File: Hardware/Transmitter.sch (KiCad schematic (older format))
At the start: 26 parts, among them U2 ADF7012, X1 VCXO

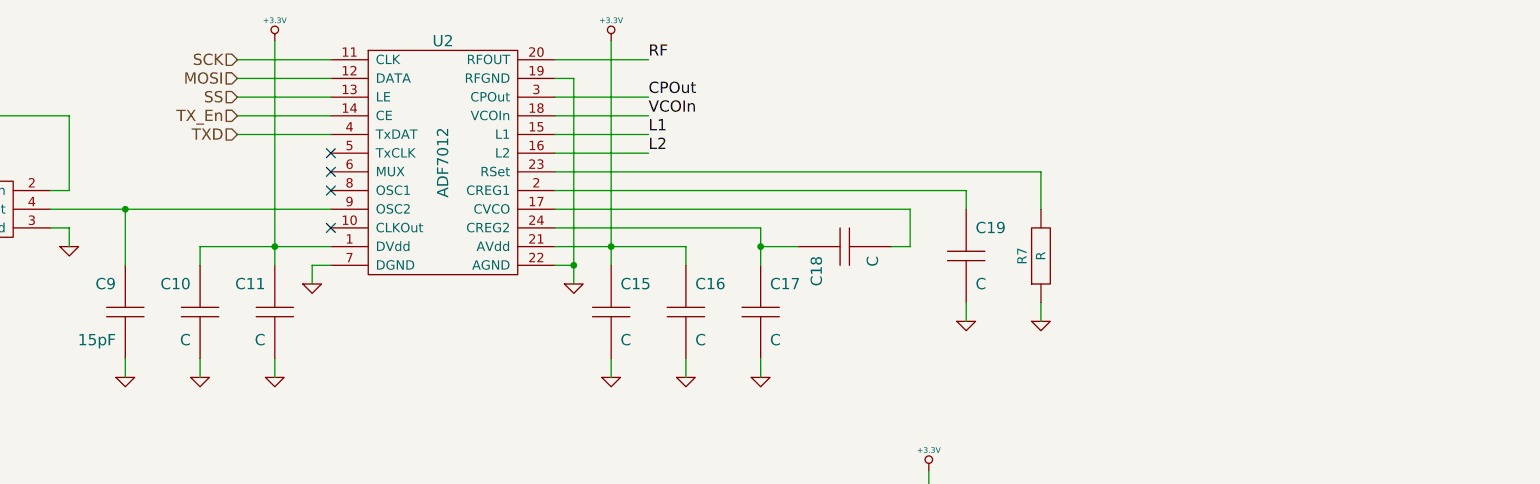
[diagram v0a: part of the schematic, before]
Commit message: Transmitter support components
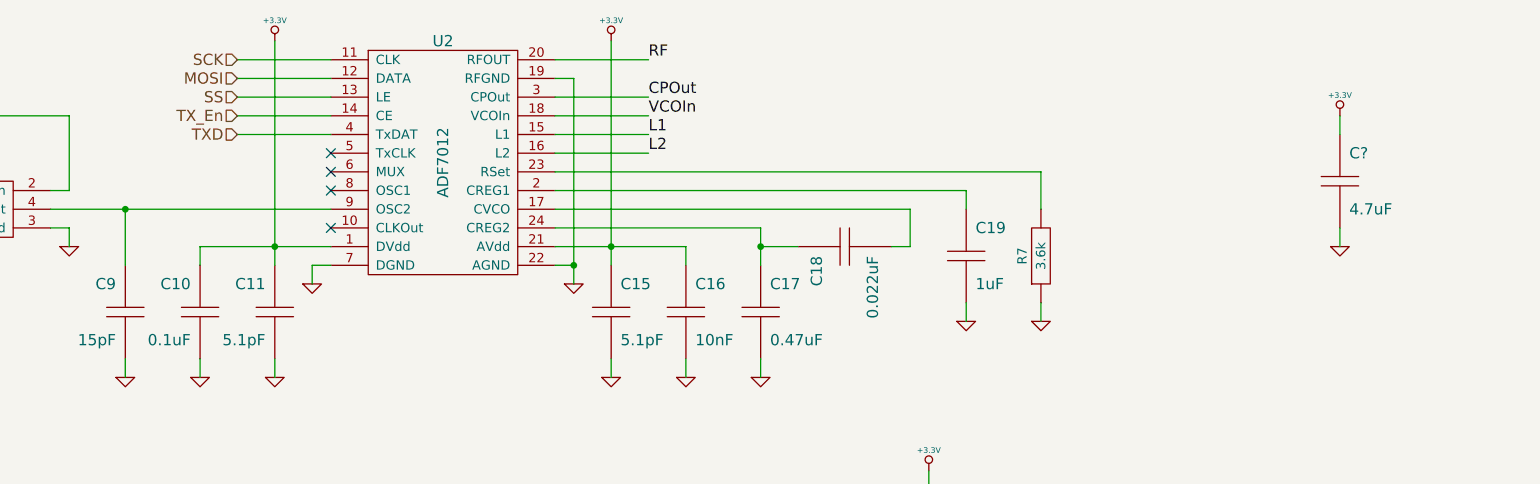
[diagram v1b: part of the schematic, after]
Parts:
- added C?: 4.7uF, CAPC2012-N, symbol C
- C10: value C -> 0.1uF; footprint ~ -> CAPC1005-N; Dielectric D -> X7R; Distributor Part No (none) -> 1276-1001-1-ND; MFR Name (none) -> Samsung; MFR Part No (none) -> CL05B104KO5NNNC; Voltage V -> 16V
- C11, C15: value C -> 5.1pF; footprint ~ -> CAPC1005-N; Dielectric D -> NP0; Distributor Part No (none) -> 490-5945-1-ND; MFR Name (none) -> Murata; MFR Part No (none) -> GRM1555C1H5R1DA01D; Voltage V -> 50V
- C16: value C -> 10nF; footprint ~ -> CAPC1005-N; Dielectric D -> X7R; Distributor Part No (none) -> 311-1042-1-ND; MFR Name (none) -> Yageo; MFR Part No (none) -> CC0402KRX7R7BB103; Voltage V -> 16V
- C17: value C -> 0.47uF; footprint ~ -> CAPC1005-N; Dielectric D -> X5R; Distributor Part No (none) -> 1276-1173-1-ND; MFR Name (none) -> Samsung; MFR Part No (none) -> CL05A474KP5NNNC; Voltage V -> 10V
- C18: value C -> 0.022uF; footprint ~ -> CAPC1005-N; Dielectric D -> X7R; Distributor Part No (none) -> 587-2239-1-ND; MFR Name (none) -> Taiyo Yuden; MFR Part No (none) -> TMK105B7223KV-F; Voltage V -> 25V
- C19: value C -> 1uF; footprint ~ -> CAPC1005-N; Dielectric D -> X7R; Distributor Part No (none) -> 587-1242-1-ND; MFR Name (none) -> Taiyo Yuden; MFR Part No (none) -> LMK107B7105KA-T; Voltage V -> 10V
- C8: Dielectric D -> X7R; Distributor Part No (none) -> 1276-1001-1-ND; MFR Name (none) -> Samsung; MFR Part No (none) -> CL05B104KO5NNNC; Voltage V -> 16V
- C9: footprint ~ -> CAPC1005-N; Dielectric D -> NP0; Distributor Part No (none) -> 1276-1179-1-ND; MFR Name (none) -> Samsung; MFR Part No (none) -> CL05C150JB5NNNC; Voltage V -> 50V
- R7: value R -> 3.6k; footprint ~ -> RESC1005-N; Distributor Part No (none) -> 311-3.6KJRCT-ND; MFR Name (none) -> Yageo; MFR Part No (none) -> RC0402JR-073K6L; Power W -> 1/16W; Tolerance % -> 5%
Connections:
- net +3.3V: now also C?.1
- net GND: now also C?.2
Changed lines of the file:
@@
 Sheet 3 4
 Title "Aether - Pico Tracker"
-Date "7 feb 2014"
+Date "8 feb 2014"
 Rev "1"
 Comp "Aerodyne Labs"
@@
 P 7700 3650
 F 0 "R7" H 7700 3750 50  0000 C CNN
-F 1 "R" H 7700 3650 50  0000 C CNN
-F 2 "~" H 7700 3650 60  0000 C CNN
+F 1 "3.6k" H 7700 3650 50  0000 C CNN
+F 2 "RESC1005-N" H 7700 3650 60  0001 C CNN
 F 3 "~" H 7700 3650 60  0000 C CNN
-F 4 "W" H 7700 3550 50  0001 C CNN "Power"
-F 5 "%" H 7700 3450 50  0001 C CNN "Tolerance"
+F 4 "Yageo" H 7700 3650 60  0001 C CNN "MFR Name"
+F 5 "RC0402JR-073K6L" H 7700 3650 60  0001 C CNN "MFR Part No"
+F 6 "311-3.6KJRCT-ND" H 7700 3650 60  0001 C CNN "Distributor Part No"
+F 7 "1/16W" H 7700 3550 50  0001 C CNN "Power"
+F 8 "5%" H 7700 3450 50  0001 C CNN "Tolerance"
 	1    7700 3650
 	0    -1   -1   0
@@
 P 7300 3650
 F 0 "C19" H 7350 3800 60  0000 L CNN
-F 1 "C" H 7350 3500 60  0000 L CNN
-F 2 "~" H 7300 3650 60  0000 C CNN
+F 1 "1uF" H 7350 3500 60  0000 L CNN
+F 2 "CAPC1005-N" H 7300 3650 60  0001 C CNN
 F 3 "~" H 7300 3650 60  0000 C CNN
-F 4 "V" H 7250 3500 60  0001 R CNN "Voltage"
-F 5 "D" H 7250 3800 60  0001 R CNN "Dielectric"
+F 4 "Taiyo Yuden" H 7300 3650 60  0001 C CNN "MFR Name"
+F 5 "LMK107B7105KA-T" H 7300 3650 60  0001 C CNN "MFR Part No"
+F 6 "587-1242-1-ND" H 7300 3650 60  0001 C CNN "Distributor Part No"
+F 7 "10V" H 7250 3500 60  0001 R CNN "Voltage"
+F 8 "X7R" H 7250 3800 60  0001 R CNN "Dielectric"
 	1    7300 3650
 	1    0    0    -1
@@
 P 6650 3600
 F 0 "C18" H 6700 3750 60  0000 L CNN
-F 1 "C" H 6700 3450 60  0000 L CNN
-F 2 "~" H 6650 3600 60  0000 C CNN
+F 1 "0.022uF" H 6700 3450 60  0000 L CNN
+F 2 "CAPC1005-N" H 6650 3600 60  0001 C CNN
 F 3 "~" H 6650 3600 60  0000 C CNN
-F 4 "V" H 6600 3450 60  0001 R CNN "Voltage"
-F 5 "D" H 6600 3750 60  0001 R CNN "Dielectric"
+F 4 "Taiyo Yuden" H 6650 3600 60  0001 C CNN "MFR Name"
+F 5 "TMK105B7223KV-F" H 6650 3600 60  0001 C CNN "MFR Part No"
+F 6 "587-2239-1-ND" H 6650 3600 60  0001 C CNN "Distributor Part No"
+F 7 "25V" H 6600 3450 60  0001 R CNN "Voltage"
+F 8 "X7R" H 6600 3750 60  0001 R CNN "Dielectric"
 	1    6650 3600
 	0    -1   1    0
@@
 P 6200 3950
 F 0 "C17" H 6250 4100 60  0000 L CNN
-F 1 "C" H 6250 3800 60  0000 L CNN
-F 2 "~" H 6200 3950 60  0000 C CNN
+F 1 "0.47uF" H 6250 3800 60  0000 L CNN
+F 2 "CAPC1005-N" H 6200 3950 60  0001 C CNN
 F 3 "~" H 6200 3950 60  0000 C CNN
-F 4 "V" H 6150 3800 60  0001 R CNN "Voltage"
-F 5 "D" H 6150 4100 60  0001 R CNN "Dielectric"
+F 4 "Samsung" H 6200 3950 60  0001 C CNN "MFR Name"
+F 5 "CL05A474KP5NNNC" H 6200 3950 60  0001 C CNN "MFR Part No"
+F 6 "1276-1173-1-ND" H 6200 3950 60  0001 C CNN "Distributor Part No"
+F 7 "10V" H 6150 3800 60  0001 R CNN "Voltage"
+F 8 "X5R" H 6150 4100 60  0001 R CNN "Dielectric"
 	1    6200 3950
-	1    0    0    -1
-$EndComp
-$Comp
-L C C15
-U 1 1 52E9CC2A
-P 5400 3950
-F 0 "C15" H 5450 4100 60  0000 L CNN
-F 1 "C" H 5450 3800 60  0000 L CNN
-F 2 "~" H 5400 3950 60  0000 C CNN
-F 3 "~" H 5400 3950 60  0000 C CNN
-F 4 "V" H 5350 3800 60  0001 R CNN "Voltage"
-F 5 "D" H 5350 4100 60  0001 R CNN "Dielectric"
-	1    5400 3950
 	1    0    0    -1
 $EndComp
@@
 P 3600 3950
 F 0 "C11" H 3650 4100 60  0000 L CNN
-F 1 "C" H 3650 3800 60  0000 L CNN
-F 2 "~" H 3600 3950 60  0000 C CNN
+F 1 "5.1pF" H 3650 3800 60  0000 L CNN
+F 2 "CAPC1005-N" H 3600 3950 60  0001 C CNN
 F 3 "~" H 3600 3950 60  0000 C CNN
-F 4 "V" H 3550 3800 60  0001 R CNN "Voltage"
-F 5 "D" H 3550 4100 60  0001 R CNN "Dielectric"
+F 4 "Murata" H 3600 3950 60  0001 C CNN "MFR Name"
+F 5 "GRM1555C1H5R1DA01D" H 3600 3950 60  0001 C CNN "MFR Part No"
+F 6 "490-5945-1-ND" H 3600 3950 60  0001 C CNN "Distributor Part No"
+F 7 "50V" H 3550 3800 60  0001 R CNN "Voltage"
+F 8 "NP0" H 3550 4100 60  0001 R CNN "Dielectric"
 	1    3600 3950
 	-1   0    0    -1
@@
 P 5800 3950
 F 0 "C16" H 5850 4100 60  0000 L CNN
-F 1 "C" H 5850 3800 60  0000 L CNN
-F 2 "~" H 5800 3950 60  0000 C CNN
+F 1 "10nF" H 5850 3800 60  0000 L CNN
+F 2 "CAPC1005-N" H 5800 3950 60  0001 C CNN
 F 3 "~" H 5800 3950 60  0000 C CNN
-F 4 "V" H 5750 3800 60  0001 R CNN "Voltage"
-F 5 "D" H 5750 4100 60  0001 R CNN "Dielectric"
+F 4 "Yageo" H 5800 3950 60  0001 C CNN "MFR Name"
+F 5 "CC0402KRX7R7BB103" H 5800 3950 60  0001 C CNN "MFR Part No"
+F 6 "311-1042-1-ND" H 5800 3950 60  0001 C CNN "Distributor Part No"
+F 7 "16V" H 5750 3800 60  0001 R CNN "Voltage"
+F 8 "X7R" H 5750 4100 60  0001 R CNN "Dielectric"
 	1    5800 3950
 	1    0    0    -1
-$EndComp
-$Comp
-L C C10
-U 1 1 52E9CD13
-P 3200 3950
-F 0 "C10" H 3250 4100 60  0000 L CNN
-F 1 "C" H 3250 3800 60  0000 L CNN
-F 2 "~" H 3200 3950 60  0000 C CNN
-F 3 "~" H 3200 3950 60  0000 C CNN
-F 4 "V" H 3150 3800 60  0001 R CNN "Voltage"
-F 5 "D" H 3150 4100 60  0001 R CNN "Dielectric"
-	1    3200 3950
-	-1   0    0    -1
 $EndComp
 $Comp
@@
 F 0 "C9" H 2850 4100 60  0000 L CNN
 F 1 "15pF" H 2850 3800 60  0000 L CNN
-F 2 "~" H 2800 3950 60  0000 C CNN
+F 2 "CAPC1005-N" H 2800 3950 60  0001 C CNN
 F 3 "~" H 2800 3950 60  0000 C CNN
-F 4 "V" H 2750 3800 60  0001 R CNN "Voltage"
-F 5 "D" H 2750 4100 60  0001 R CNN "Dielectric"
+F 4 "Samsung" H 2800 3950 60  0001 C CNN "MFR Name"
+F 5 "CL05C150JB5NNNC" H 2800 3950 60  0001 C CNN "MFR Part No"
+F 6 "1276-1179-1-ND" H 2800 3950 60  0001 C CNN "Distributor Part No"
+F 7 "50V" H 2750 3800 60  0001 R CNN "Voltage"
+F 8 "NP0" H 2750 4100 60  0001 R CNN "Dielectric"
 	1    2800 3950
 	-1   0    0    -1
@@
 F 2 "CAPC1005-N" H 1100 3850 60  0001 C CNN
 F 3 "~" H 1100 3850 60  0000 C CNN
-F 4 "V" H 1050 3700 60  0001 R CNN "Voltage"
-F 5 "D" H 1050 4000 60  0001 R CNN "Dielectric"
+F 4 "Samsung" H 1100 3850 60  0001 C CNN "MFR Name"
+F 5 "CL05B104KO5NNNC" H 1100 3850 60  0001 C CNN "MFR Part No"
+F 6 "1276-1001-1-ND" H 1100 3850 60  0001 C CNN "Distributor Part No"
+F 7 "16V" H 1050 3700 60  0001 R CNN "Voltage"
+F 8 "X7R" H 1050 4000 60  0001 R CNN "Dielectric"
 	1    1100 3850
 	1    0    0    -1
@@
 	1    0    0    -1
 $EndComp
+$Comp
+L C C?
+U 1 1 52F58959
+P 9300 3250
+F 0 "C?" H 9350 3400 60  0000 L CNN
+F 1 "4.7uF" H 9350 3100 60  0000 L CNN
+F 2 "CAPC2012-N" H 9300 3250 60  0001 C CNN
+F 3 "~" H 9300 3250 60  0000 C CNN
+F 4 "Samsung" H 9300 3250 60  0001 C CNN "MFR Name"
+F 5 "CL21A475KOFNNNE" H 9300 3250 60  0001 C CNN "MFR Part No"
+F 6 "1276-1065-1-ND" H 9300 3250 60  0001 C CNN "Distributor Part No"
+F 7 "16V" H 9250 3100 60  0001 R CNN "Voltage"
+F 8 "X5R" H 9250 3400 60  0001 R CNN "Dielectric"
+	1    9300 3250
+	1    0    0    -1
+$EndComp
+$Comp
+L +3.3V #PWR?
+U 1 1 52F58974
+P 9300 2900
+F 0 "#PWR?" H 9300 2860 30  0001 C CNN
+F 1 "+3.3V" H 9300 3010 30  0000 C CNN
+F 2 "" H 9300 2900 60  0000 C CNN
+F 3 "" H 9300 2900 60  0000 C CNN
+	1    9300 2900
+	1    0    0    -1
+$EndComp
+$Comp
+L GND #PWR?
+U 1 1 52F58983
+P 9300 3600
+F 0 "#PWR?" H 9300 3600 30  0001 C CNN
+F 1 "GND" H 9300 3530 30  0001 C CNN
+F 2 "" H 9300 3600 60  0000 C CNN
+F 3 "" H 9300 3600 60  0000 C CNN
+	1    9300 3600
+	1    0    0    -1
+$EndComp
+Wire Wire Line
+	9300 3600 9300 3500
+Wire Wire Line
+	9300 2900 9300 3000
+$Comp
+L C C10
+U 1 1 52F58E90
+P 3200 3950
+F 0 "C10" H 3250 4100 60  0000 L CNN
+F 1 "0.1uF" H 3250 3800 60  0000 L CNN
+F 2 "CAPC1005-N" H 3200 3950 60  0001 C CNN
+F 3 "~" H 3200 3950 60  0000 C CNN
+F 4 "Samsung" H 3200 3950 60  0001 C CNN "MFR Name"
+F 5 "CL05B104KO5NNNC" H 3200 3950 60  0001 C CNN "MFR Part No"
+F 6 "1276-1001-1-ND" H 3200 3950 60  0001 C CNN "Distributor Part No"
+F 7 "16V" H 3150 3800 60  0001 R CNN "Voltage"
+F 8 "X7R" H 3150 4100 60  0001 R CNN "Dielectric"
+	1    3200 3950
+	-1   0    0    -1
+$EndComp
+$Comp
+L C C15
+U 1 1 52F58F64
+P 5400 3950
+F 0 "C15" H 5450 4100 60  0000 L CNN
+F 1 "5.1pF" H 5450 3800 60  0000 L CNN
+F 2 "CAPC1005-N" H 5400 3950 60  0001 C CNN
+F 3 "~" H 5400 3950 60  0000 C CNN
+F 4 "Murata" H 5400 3950 60  0001 C CNN "MFR Name"
+F 5 "GRM1555C1H5R1DA01D" H 5400 3950 60  0001 C CNN "MFR Part No"
+F 6 "490-5945-1-ND" H 5400 3950 60  0001 C CNN "Distributor Part No"
+F 7 "50V" H 5350 3800 60  0001 R CNN "Voltage"
+F 8 "NP0" H 5350 4100 60  0001 R CNN "Dielectric"
+	1    5400 3950
+	1    0    0    -1
+$EndComp

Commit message: Voltage regulator components
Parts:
- gave numbers to parts that had none: 1
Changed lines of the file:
@@
 $EndComp
 $Comp
-L C C?
+L C C35
 U 1 1 52F58959
 P 9300 3250
-F 0 "C?" H 9350 3400 60  0000 L CNN
+F 0 "C35" H 9350 3400 60  0000 L CNN
 F 1 "4.7uF" H 9350 3100 60  0000 L CNN
 F 2 "CAPC2012-N" H 9300 3250 60  0001 C CNN
@@
 $EndComp
 $Comp
-L +3.3V #PWR?
+L +3.3V #PWR048
 U 1 1 52F58974
 P 9300 2900
-F 0 "#PWR?" H 9300 2860 30  0001 C CNN
+F 0 "#PWR048" H 9300 2860 30  0001 C CNN
 F 1 "+3.3V" H 9300 3010 30  0000 C CNN
 F 2 "" H 9300 2900 60  0000 C CNN
@@
 $EndComp
 $Comp
-L GND #PWR?
+L GND #PWR049
 U 1 1 52F58983
 P 9300 3600
-F 0 "#PWR?" H 9300 3600 30  0001 C CNN
+F 0 "#PWR049" H 9300 3600 30  0001 C CNN
 F 1 "GND" H 9300 3530 30  0001 C CNN
 F 2 "" H 9300 3600 60  0000 C CNN

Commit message: Consolidate LED resistors
See #1
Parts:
- C20: footprint ~ -> CAPC1005-N; Dielectric D -> X7R; Distributor Part No (none) -> 311-1028-1-ND; MFR Name (none) -> Yageo; MFR Part No (none) -> CC0402KRX7R9BB471; Voltage V -> 50V
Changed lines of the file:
@@
 $Descr A4 11693 8268
 encoding utf-8
-Sheet 3 4
+Sheet 2 4
 Title "Aether - Pico Tracker"
-Date "9 feb 2014"
+Date "24 feb 2014"
 Rev "1"
 Comp "Aerodyne Labs"
@@
 F 0 "C20" H 8300 5850 60  0000 L CNN
 F 1 "470pF" H 8300 5550 60  0000 L CNN
-F 2 "~" H 8250 5700 60  0000 C CNN
+F 2 "CAPC1005-N" H 8250 5700 60  0001 C CNN
 F 3 "~" H 8250 5700 60  0000 C CNN
-F 4 "V" H 8200 5550 60  0001 R CNN "Voltage"
-F 5 "D" H 8200 5850 60  0001 R CNN "Dielectric"
+F 4 "Yageo" H 8250 5700 60  0001 C CNN "MFR Name"
+F 5 "CC0402KRX7R9BB471" H 8250 5700 60  0001 C CNN "MFR Part No"
+F 6 "311-1028-1-ND" H 8250 5700 60  0001 C CNN "Distributor Part No"
+F 7 "50V" H 8200 5550 60  0001 R CNN "Voltage"
+F 8 "X7R" H 8200 5850 60  0001 R CNN "Dielectric"
 	1    8250 5700
 	0    -1   -1   0

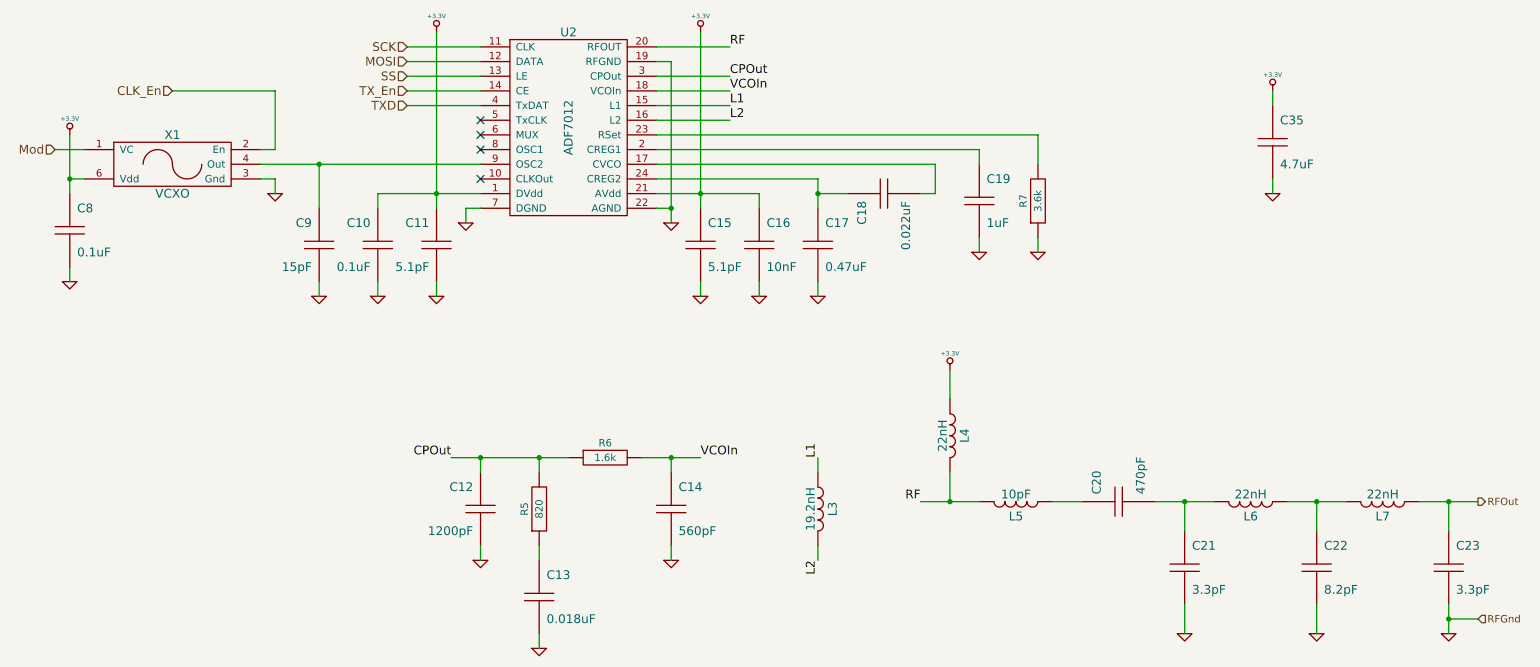
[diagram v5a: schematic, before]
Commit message: Prepare for r2
Delete board, netlist, associations
Clear annotations
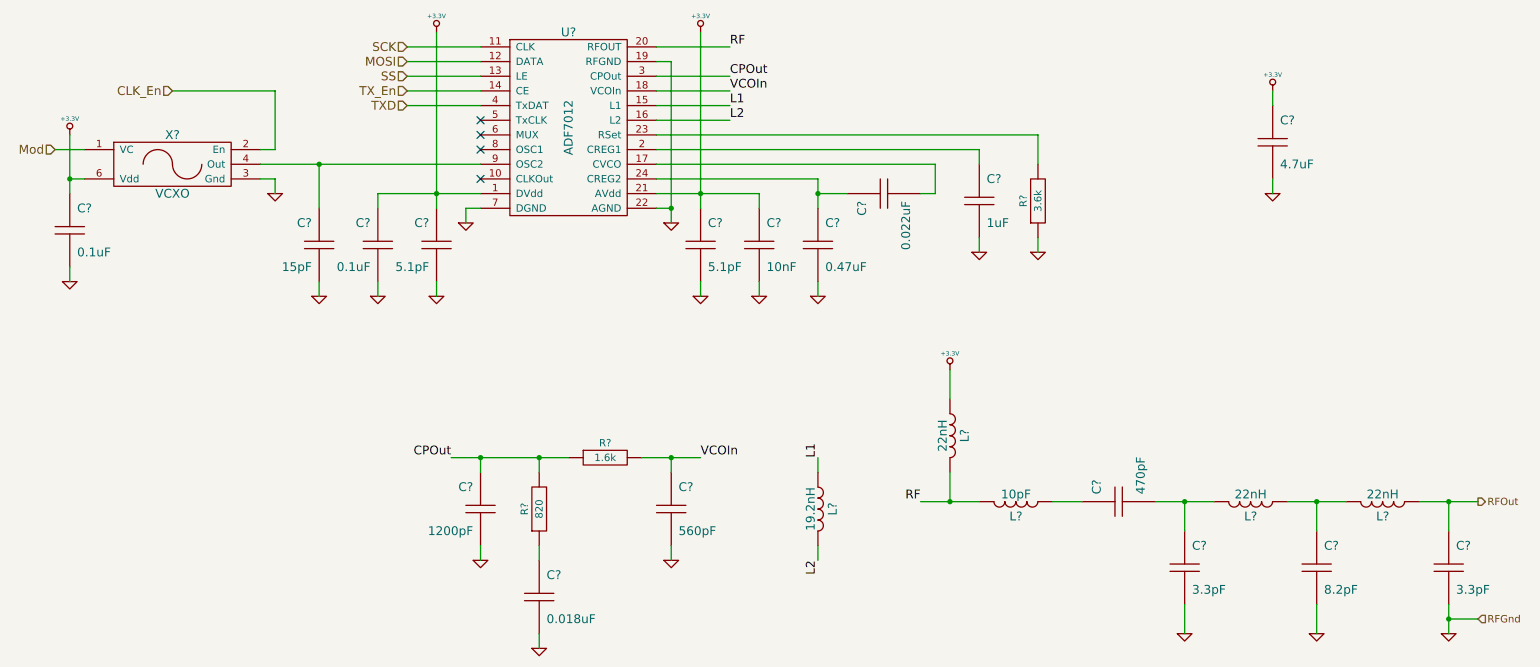
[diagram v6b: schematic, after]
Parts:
- renumbered C19 to C?, C18 to C?, C17 to C?, C11 to C?, C16 to C?, C12 to C?, C13 to C?, C14 to C?, C20 to C?, C21 to C?, C22 to C?, C9 to C?, C8 to C?, C23 to C?, C35 to C?, C10 to C?, C15 to C?, L3 to L?, L5 to L?, L6 to L?, L7 to L?, L4 to L?, R7 to R?, R5 to R?, R6 to R?, U2 to U?, X1 to X?

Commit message: Remove old transmitter
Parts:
- removed C?: 1uF, CAPC1005-N, symbol C
- removed C?: 0.022uF, CAPC1005-N, symbol C
- removed C?: 0.47uF, CAPC1005-N, symbol C
- removed C? (x2): 5.1pF, CAPC1005-N, symbol C
- removed C?: 10nF, CAPC1005-N, symbol C
- removed C?: 1200pF, CAPC1005-N, symbol C
- removed C?: 0.018uF, CAPC1005-N, symbol C
- removed C?: 560pF, CAPC1005-N, symbol C
- removed C?: 470pF, CAPC1005-N, symbol C
- removed C? (x2): 3.3pF, CAPC1005-N, symbol C
- removed C?: 8.2pF, CAPC1005-N, symbol C
- removed C?: 15pF, CAPC1005-N, symbol C
- removed C? (x2): 0.1uF, CAPC1005-N, symbol C
- removed C?: 4.7uF, CAPC2012-N, symbol C
- removed L?: 19.2nH, INDC1005-N, symbol L
- removed L?: 10pF, INDC1005-N, symbol L
- removed L? (x3): 22nH, INDC1005-N, symbol L
- removed R?: 3.6k, RESC1005-N, symbol R
- removed R?: 820, RESC1005-N, symbol R
- removed R?: 1.6k, RESC1005-N, symbol R
- removed U?: ADF7012, symbol ADF7012
- removed X?: VCXO, OSCSC254P750X520-6N, symbol VCXO
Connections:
- no-connect marks 4 -> 0
